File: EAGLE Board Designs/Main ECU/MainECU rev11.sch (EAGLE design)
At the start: 208 parts, among them J1 CONNECTOR-40__, J2 ADIS16460, J3 CONNECTOR-40__, J4 CONNECTOR-40__, J5 CONNECTOR-40__, K1 RELAY_DPDT_RT424024, K10 RELAY_DPDT_RT424024, K11 RELAY_DPDT_RT424024, K12 RELAY_DPDT_RT424024, K9 RELAY_DPDT_RT424024, Q3 TRANSISTOR_P_MOS_SOT-23_DMP30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, Q4 TRANSISTOR_N_MOS__DMG3406L-7, Q5 TRANSISTOR_P_MOS_SOT-23_DMP30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, Q6 TRANSISTOR_N_MOS__DMG3406L-7, U1 VOLTAGE_REGULATOR_SOT-223_3.3V, U2 TCAN1051HQV-Q1, U23 ADC128S022, U3 TCAN1051HQV-Q1, U32 ADC128S022, U33 TCAN1051HQV-Q1, U34 OPAMP_1_CHANNEL_OPA991, U37 OPAMP_1_CHANNEL_OPA991, U38 LOGICGATE_OR, U39 OPAMP_1_CHANNEL_OPA991, U4 TCAN1051HQV-Q1, U41 OPAMP_1_CHANNEL_OPA991, U42 LOGICGATE_OR, U43 OPAMP_1_CHANNEL_OPA991, U44 LOGICGATE_NAND, U45 TCAN1051HQV-Q1, U46 TCAN1051HQV-Q1, U5 ADM8316WBX30, U6 ADC128S022, U7 ADC128S022

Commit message: routing progress
routing progress

routing progress
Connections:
- net +24V: now also J1.15, J1.16; no longer J1.1, J1.2
- net +5V: now also J1.14; no longer J1.3, J1.4
- net CANH_1: now also J1.12, U33.CANH; no longer J3.13
- net CANH_2: now also J1.8; no longer J3.16
- net CANH_3: now also J1.4; no longer J3.19, U33.CANH
- net CANL_1: now also J1.10, U33.CANL; no longer J3.14
- net CANL_2: now also J1.6; no longer J3.17
- net CANL_3: now also J1.2; no longer J3.20, U33.CANL
- net CURRENT: now also U32.IN1
- net CURRENT_EXT: no longer U32.IN1
- net GND: no longer J1.5
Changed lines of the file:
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@@
 <attribute name="DESCRIPTION_2" x="176.53" y="10.16" size="2.54" layer="95"/>
 </instance>
-<instance part="U$8" gate="G$1" x="43.18" y="203.2" smashed="yes">
-<attribute name="VALUE" x="43.18" y="208.28" size="1.778" layer="96" align="bottom-center"/>
+<instance part="U$8" gate="G$1" x="78.74" y="167.64" smashed="yes">
+<attribute name="VALUE" x="78.74" y="172.72" size="1.778" layer="96" align="bottom-center"/>
 </instance>
 <instance part="P46" gate="1" x="160.02" y="203.2" smashed="yes">
@@
 <attribute name="VALUE" x="137.16" y="92.71" size="1.27" layer="96" align="top-center"/>
 </instance>
-<instance part="P70" gate="1" x="50.8" y="203.2" smashed="yes">
-<attribute name="VALUE" x="50.8" y="205.74" size="1.27" layer="96" align="bottom-center"/>
+<instance part="P70" gate="1" x="73.66" y="170.18" smashed="yes">
+<attribute name="VALUE" x="73.66" y="172.72" size="1.27" layer="96" align="bottom-center"/>
 </instance>
 <instance part="J1" gate="G$1" x="30.48" y="200.66" smashed="yes">
@@
 </busses>
 <nets>
-<net name="+24V" class="0">
-<segment>
-<pinref part="U$8" gate="G$1" pin="+24V"/>
-<wire x1="40.64" y1="195.58" x2="43.18" y2="195.58" width="0.1524" layer="91"/>
-<wire x1="43.18" y1="195.58" x2="43.18" y2="198.12" width="0.1524" layer="91"/>
-<wire x1="43.18" y1="198.12" x2="43.18" y2="200.66" width="0.1524" layer="91"/>
-<wire x1="40.64" y1="198.12" x2="43.18" y2="198.12" width="0.1524" layer="91"/>
-<junction x="43.18" y="198.12"/>
-<pinref part="J1" gate="G$1" pin="1"/>
-<pinref part="J1" gate="G$1" pin="2"/>
-</segment>
-</net>
 <net name="LOAD_FR_EXT" class="0">
 <segment>
@@
 <segment>
 <pinref part="P64" gate="1" pin="GND"/>
-<wire x1="40.64" y1="187.96" x2="78.74" y2="187.96" width="0.1524" layer="91"/>
-<pinref part="J1" gate="G$1" pin="5"/>
-<wire x1="78.74" y1="187.96" x2="78.74" y2="157.48" width="0.1524" layer="91"/>
 <pinref part="J1" gate="G$1" pin="22"/>
 <wire x1="78.74" y1="157.48" x2="78.74" y2="154.94" width="0.1524" layer="91"/>
@@
 <pinref part="J1" gate="G$1" pin="17"/>
 <wire x1="40.64" y1="157.48" x2="78.74" y2="157.48" width="0.1524" layer="91"/>
-<junction x="78.74" y="157.48"/>
 </segment>
 <segment>
@@
 <net name="CANH_1" class="0">
 <segment>
-<wire x1="99.06" y1="167.64" x2="106.68" y2="167.64" width="0.1524" layer="91"/>
-<label x="106.68" y="167.64" size="1.27" layer="95" xref="yes"/>
-<pinref part="J3" gate="G$1" pin="13"/>
+<wire x1="40.64" y1="170.18" x2="48.26" y2="170.18" width="0.1524" layer="91"/>
+<label x="48.26" y="170.18" size="1.27" layer="95" xref="yes"/>
+<pinref part="J1" gate="G$1" pin="12"/>
 </segment>
 </net>
 <net name="CANL_1" class="0">
 <segment>
-<wire x1="99.06" y1="165.1" x2="106.68" y2="165.1" width="0.1524" layer="91"/>
-<label x="106.68" y="165.1" size="1.27" layer="95" xref="yes"/>
-<pinref part="J3" gate="G$1" pin="14"/>
+<wire x1="40.64" y1="175.26" x2="48.26" y2="175.26" width="0.1524" layer="91"/>
+<label x="48.26" y="175.26" size="1.27" layer="95" xref="yes"/>
+<pinref part="J1" gate="G$1" pin="10"/>
 </segment>
 </net>
 <net name="CANH_2" class="0">
 <segment>
-<wire x1="99.06" y1="160.02" x2="106.68" y2="160.02" width="0.1524" layer="91"/>
-<label x="106.68" y="160.02" size="1.27" layer="95" xref="yes"/>
-<pinref part="J3" gate="G$1" pin="16"/>
+<wire x1="40.64" y1="180.34" x2="48.26" y2="180.34" width="0.1524" layer="91"/>
+<label x="48.26" y="180.34" size="1.27" layer="95" xref="yes"/>
+<pinref part="J1" gate="G$1" pin="8"/>
 </segment>
 </net>
 <net name="CANL_2" class="0">
 <segment>
-<wire x1="99.06" y1="157.48" x2="106.68" y2="157.48" width="0.1524" layer="91"/>
-<label x="106.68" y="157.48" size="1.27" layer="95" xref="yes"/>
-<pinref part="J3" gate="G$1" pin="17"/>
+<wire x1="40.64" y1="185.42" x2="48.26" y2="185.42" width="0.1524" layer="91"/>
+<label x="48.26" y="185.42" size="1.27" layer="95" xref="yes"/>
+<pinref part="J1" gate="G$1" pin="6"/>
 </segment>
 </net>
 <net name="CANH_3" class="0">
 <segment>
-<wire x1="99.06" y1="152.4" x2="106.68" y2="152.4" width="0.1524" layer="91"/>
-<label x="106.68" y="152.4" size="1.27" layer="95" xref="yes"/>
-<pinref part="J3" gate="G$1" pin="19"/>
+<wire x1="40.64" y1="190.5" x2="48.26" y2="190.5" width="0.1524" layer="91"/>
+<pinref part="J1" gate="G$1" pin="4"/>
+<label x="48.26" y="190.5" size="1.27" layer="95" xref="yes"/>
 </segment>
 </net>
 <net name="CANL_3" class="0">
 <segment>
-<wire x1="99.06" y1="149.86" x2="106.68" y2="149.86" width="0.1524" layer="91"/>
-<label x="106.68" y="149.86" size="1.27" layer="95" xref="yes"/>
-<pinref part="J3" gate="G$1" pin="20"/>
+<wire x1="40.64" y1="195.58" x2="48.26" y2="195.58" width="0.1524" layer="91"/>
+<pinref part="J1" gate="G$1" pin="2"/>
+<label x="48.26" y="195.58" size="1.27" layer="95" xref="yes"/>
 </segment>
 </net>
@@
 <net name="INVERTER_24V_EN" class="0">
 <segment>
-<wire x1="43.18" y1="170.18" x2="50.8" y2="170.18" width="0.1524" layer="91"/>
-<label x="50.8" y="170.18" size="1.27" layer="95" xref="yes"/>
+<wire x1="5.08" y1="236.22" x2="12.7" y2="236.22" width="0.1524" layer="91"/>
+<label x="12.7" y="236.22" size="1.27" layer="95" xref="yes"/>
 </segment>
 </net>
 <net name="INVERTER_TORQUE_EN" class="0">
 <segment>
-<wire x1="43.18" y1="167.64" x2="50.8" y2="167.64" width="0.1524" layer="91"/>
-<label x="50.8" y="167.64" size="1.27" layer="95" xref="yes"/>
+<wire x1="5.08" y1="233.68" x2="12.7" y2="233.68" width="0.1524" layer="91"/>
+<label x="12.7" y="233.68" size="1.27" layer="95" xref="yes"/>
 </segment>
 </net>
 <net name="INVERTER_OUTPUT_EN" class="0">
 <segment>
-<wire x1="43.18" y1="165.1" x2="50.8" y2="165.1" width="0.1524" layer="91"/>
-<label x="50.8" y="165.1" size="1.27" layer="95" xref="yes"/>
+<wire x1="5.08" y1="231.14" x2="12.7" y2="231.14" width="0.1524" layer="91"/>
+<label x="12.7" y="231.14" size="1.27" layer="95" xref="yes"/>
 </segment>
 </net>
 <net name="INVERTER_CTL_EN" class="0">
 <segment>
-<wire x1="43.18" y1="162.56" x2="50.8" y2="162.56" width="0.1524" layer="91"/>
-<label x="50.8" y="162.56" size="1.27" layer="95" xref="yes"/>
+<wire x1="5.08" y1="228.6" x2="12.7" y2="228.6" width="0.1524" layer="91"/>
+<label x="12.7" y="228.6" size="1.27" layer="95" xref="yes"/>
 </segment>
 </net>
 <net name="BRAKE_LIGHT_EN" class="0">
 <segment>
-<wire x1="43.18" y1="160.02" x2="50.8" y2="160.02" width="0.1524" layer="91"/>
-<label x="50.8" y="160.02" size="1.27" layer="95" xref="yes"/>
+<wire x1="5.08" y1="226.06" x2="12.7" y2="226.06" width="0.1524" layer="91"/>
+<label x="12.7" y="226.06" size="1.27" layer="95" xref="yes"/>
 </segment>
 </net>
@@
 </segment>
 <segment>
+<pinref part="J1" gate="G$1" pin="14"/>
 <pinref part="P70" gate="1" pin="+5V"/>
-<wire x1="40.64" y1="193.04" x2="50.8" y2="193.04" width="0.1524" layer="91"/>
-<wire x1="50.8" y1="193.04" x2="50.8" y2="200.66" width="0.1524" layer="91"/>
-<wire x1="40.64" y1="190.5" x2="50.8" y2="190.5" width="0.1524" layer="91"/>
-<wire x1="50.8" y1="190.5" x2="50.8" y2="193.04" width="0.1524" layer="91"/>
-<junction x="50.8" y="193.04"/>
-<pinref part="J1" gate="G$1" pin="3"/>
-<pinref part="J1" gate="G$1" pin="4"/>
+<wire x1="40.64" y1="165.1" x2="73.66" y2="165.1" width="0.1524" layer="91"/>
+<wire x1="73.66" y1="165.1" x2="73.66" y2="167.64" width="0.1524" layer="91"/>
 </segment>
 </net>
@@
 </segment>
 </net>
+<net name="+24V" class="0">
+<segment>
+<pinref part="J1" gate="G$1" pin="16"/>
+<pinref part="U$8" gate="G$1" pin="+24V"/>
+<wire x1="40.64" y1="160.02" x2="78.74" y2="160.02" width="0.1524" layer="91"/>
+<wire x1="78.74" y1="160.02" x2="78.74" y2="162.56" width="0.1524" layer="91"/>
+<pinref part="J1" gate="G$1" pin="15"/>
+<wire x1="78.74" y1="162.56" x2="78.74" y2="165.1" width="0.1524" layer="91"/>
+<wire x1="40.64" y1="162.56" x2="78.74" y2="162.56" width="0.1524" layer="91"/>
+<junction x="78.74" y="162.56"/>
+</segment>
+</net>
 </nets>
 </sheet>
@@
 <net name="CANH_3" class="0">
 <segment>
-<wire x1="60.96" y1="30.48" x2="63.5" y2="30.48" width="0.1524" layer="91"/>
-<label x="63.5" y="30.48" size="1.27" layer="95" xref="yes"/>
-<pinref part="U33" gate="G$1" pin="CANH"/>
-</segment>
-<segment>
 <wire x1="187.96" y1="78.74" x2="190.5" y2="78.74" width="0.1524" layer="91"/>
 <label x="190.5" y="78.74" size="1.27" layer="95" xref="yes"/>
@@
 <net name="CANL_3" class="0">
 <segment>
-<wire x1="60.96" y1="27.94" x2="63.5" y2="27.94" width="0.1524" layer="91"/>
-<label x="63.5" y="27.94" size="1.27" layer="95" xref="yes"/>
-<pinref part="U33" gate="G$1" pin="CANL"/>
-</segment>
-<segment>
 <wire x1="187.96" y1="76.2" x2="190.5" y2="76.2" width="0.1524" layer="91"/>
 <label x="190.5" y="76.2" size="1.27" layer="95" xref="yes"/>
@@
 </segment>
 </net>
-<net name="CURRENT_EXT" class="0">
-<segment>
-<pinref part="U32" gate="G$1" pin="IN1"/>
-<wire x1="251.46" y1="93.98" x2="254" y2="93.98" width="0.1524" layer="91"/>
-<label x="254" y="93.98" size="1.27" layer="95" xref="yes"/>
-</segment>
-</net>
 <net name="TCU_RX4" class="0">
 <segment>
@@
 </segment>
 </net>
+<net name="CANH_1" class="0">
+<segment>
+<wire x1="60.96" y1="30.48" x2="63.5" y2="30.48" width="0.1524" layer="91"/>
+<label x="63.5" y="30.48" size="1.27" layer="95" xref="yes"/>
+<pinref part="U33" gate="G$1" pin="CANH"/>
+</segment>
+</net>
+<net name="CANL_1" class="0">
+<segment>
+<wire x1="60.96" y1="27.94" x2="63.5" y2="27.94" width="0.1524" layer="91"/>
+<label x="63.5" y="27.94" size="1.27" layer="95" xref="yes"/>
+<pinref part="U33" gate="G$1" pin="CANL"/>
+</segment>
+</net>
+<net name="CURRENT" class="0">
+<segment>
+<pinref part="U32" gate="G$1" pin="IN1"/>
+<wire x1="251.46" y1="93.98" x2="254" y2="93.98" width="0.1524" layer="91"/>
+<label x="254" y="93.98" size="1.27" layer="95" xref="yes"/>
+</segment>
+</net>

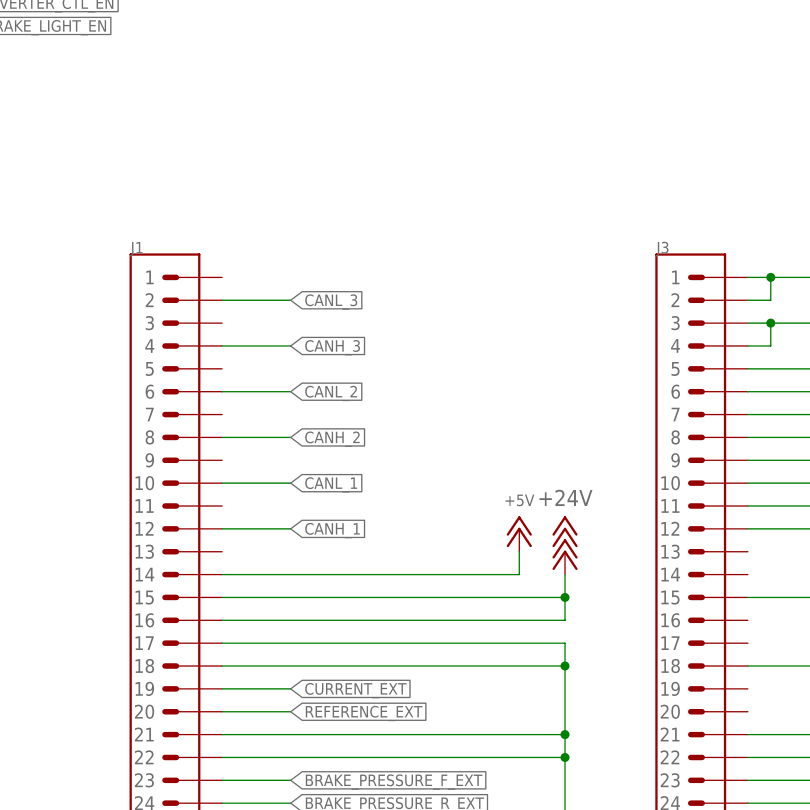
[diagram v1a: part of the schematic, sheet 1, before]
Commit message: changed orientation
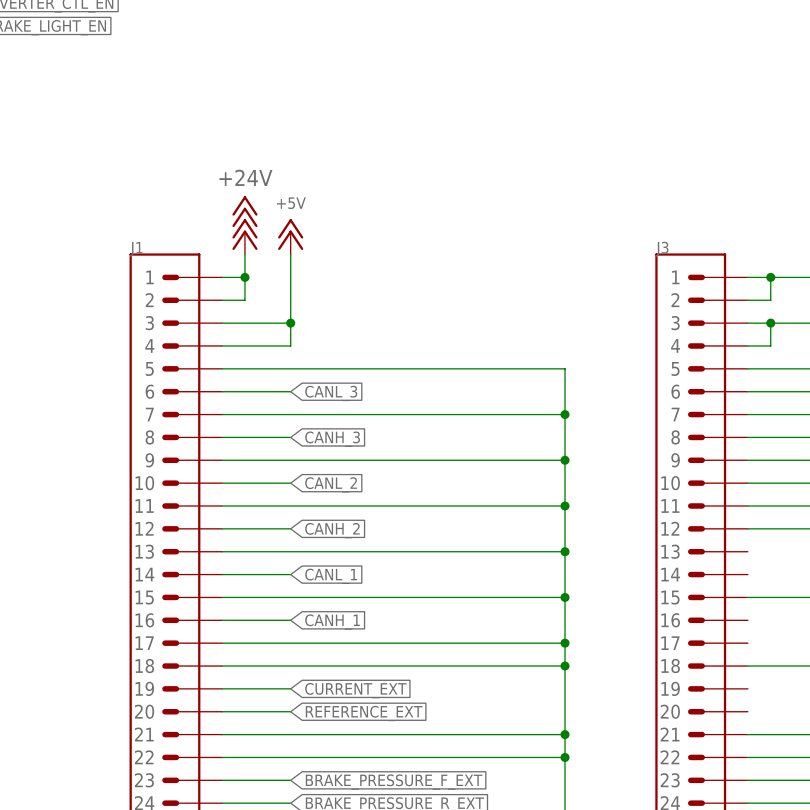
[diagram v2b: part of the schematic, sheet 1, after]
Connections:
- net +24V: now also J1.1, J1.2; no longer J1.15, J1.16
- net +5V: now also J1.3, J1.4; no longer J1.14
- net CANH_1: now also J1.16; no longer J1.12
- net CANH_2: now also J1.12; no longer J1.8
- net CANH_3: now also J1.8; no longer J1.4
- net CANL_1: now also J1.14; no longer J1.10
- net CANL_2: now also J1.10; no longer J1.6
- net CANL_3: now also J1.6; no longer J1.2
- net GND: now also J1.11, J1.13, J1.15, J1.5, J1.7, J1.9
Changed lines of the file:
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@@
 <attribute name="DESCRIPTION_2" x="176.53" y="10.16" size="2.54" layer="95"/>
 </instance>
-<instance part="U$8" gate="G$1" x="78.74" y="167.64" smashed="yes">
-<attribute name="VALUE" x="78.74" y="172.72" size="1.778" layer="96" align="bottom-center"/>
+<instance part="U$8" gate="G$1" x="43.18" y="203.2" smashed="yes">
+<attribute name="VALUE" x="43.18" y="208.28" size="1.778" layer="96" align="bottom-center"/>
 </instance>
 <instance part="P46" gate="1" x="160.02" y="203.2" smashed="yes">
@@
 <attribute name="VALUE" x="137.16" y="92.71" size="1.27" layer="96" align="top-center"/>
 </instance>
-<instance part="P70" gate="1" x="73.66" y="170.18" smashed="yes">
-<attribute name="VALUE" x="73.66" y="172.72" size="1.27" layer="96" align="bottom-center"/>
+<instance part="P70" gate="1" x="48.26" y="203.2" smashed="yes">
+<attribute name="VALUE" x="48.26" y="205.74" size="1.27" layer="96" align="bottom-center"/>
 </instance>
 <instance part="J1" gate="G$1" x="30.48" y="200.66" smashed="yes">
@@
 <pinref part="J1" gate="G$1" pin="17"/>
 <wire x1="40.64" y1="157.48" x2="78.74" y2="157.48" width="0.1524" layer="91"/>
+<pinref part="J1" gate="G$1" pin="5"/>
+<wire x1="40.64" y1="187.96" x2="78.74" y2="187.96" width="0.1524" layer="91"/>
+<wire x1="78.74" y1="187.96" x2="78.74" y2="182.88" width="0.1524" layer="91"/>
+<junction x="78.74" y="157.48"/>
+<pinref part="J1" gate="G$1" pin="7"/>
+<wire x1="78.74" y1="182.88" x2="78.74" y2="177.8" width="0.1524" layer="91"/>
+<wire x1="78.74" y1="177.8" x2="78.74" y2="172.72" width="0.1524" layer="91"/>
+<wire x1="78.74" y1="172.72" x2="78.74" y2="167.64" width="0.1524" layer="91"/>
+<wire x1="78.74" y1="167.64" x2="78.74" y2="162.56" width="0.1524" layer="91"/>
+<wire x1="78.74" y1="162.56" x2="78.74" y2="157.48" width="0.1524" layer="91"/>
+<wire x1="40.64" y1="182.88" x2="78.74" y2="182.88" width="0.1524" layer="91"/>
+<junction x="78.74" y="182.88"/>
+<pinref part="J1" gate="G$1" pin="9"/>
+<wire x1="40.64" y1="177.8" x2="78.74" y2="177.8" width="0.1524" layer="91"/>
+<junction x="78.74" y="177.8"/>
+<pinref part="J1" gate="G$1" pin="11"/>
+<wire x1="40.64" y1="172.72" x2="78.74" y2="172.72" width="0.1524" layer="91"/>
+<junction x="78.74" y="172.72"/>
+<pinref part="J1" gate="G$1" pin="13"/>
+<wire x1="40.64" y1="167.64" x2="78.74" y2="167.64" width="0.1524" layer="91"/>
+<junction x="78.74" y="167.64"/>
+<pinref part="J1" gate="G$1" pin="15"/>
+<wire x1="40.64" y1="162.56" x2="78.74" y2="162.56" width="0.1524" layer="91"/>
+<junction x="78.74" y="162.56"/>
 </segment>
 <segment>
@@
 <net name="CANH_1" class="0">
 <segment>
+<wire x1="40.64" y1="160.02" x2="48.26" y2="160.02" width="0.1524" layer="91"/>
+<label x="48.26" y="160.02" size="1.27" layer="95" xref="yes"/>
+<pinref part="J1" gate="G$1" pin="16"/>
+</segment>
+</net>
+<net name="CANL_1" class="0">
+<segment>
+<wire x1="40.64" y1="165.1" x2="48.26" y2="165.1" width="0.1524" layer="91"/>
+<label x="48.26" y="165.1" size="1.27" layer="95" xref="yes"/>
+<pinref part="J1" gate="G$1" pin="14"/>
+</segment>
+</net>
+<net name="CANH_2" class="0">
+<segment>
 <wire x1="40.64" y1="170.18" x2="48.26" y2="170.18" width="0.1524" layer="91"/>
 <label x="48.26" y="170.18" size="1.27" layer="95" xref="yes"/>
@@
 </segment>
 </net>
-<net name="CANL_1" class="0">
+<net name="CANL_2" class="0">
 <segment>
 <wire x1="40.64" y1="175.26" x2="48.26" y2="175.26" width="0.1524" layer="91"/>
@@
 </segment>
 </net>
-<net name="CANH_2" class="0">
+<net name="CANH_3" class="0">
 <segment>
 <wire x1="40.64" y1="180.34" x2="48.26" y2="180.34" width="0.1524" layer="91"/>
@@
 </segment>
 </net>
-<net name="CANL_2" class="0">
+<net name="CANL_3" class="0">
 <segment>
 <wire x1="40.64" y1="185.42" x2="48.26" y2="185.42" width="0.1524" layer="91"/>
 <label x="48.26" y="185.42" size="1.27" layer="95" xref="yes"/>
 <pinref part="J1" gate="G$1" pin="6"/>
-</segment>
-</net>
-<net name="CANH_3" class="0">
-<segment>
-<wire x1="40.64" y1="190.5" x2="48.26" y2="190.5" width="0.1524" layer="91"/>
-<pinref part="J1" gate="G$1" pin="4"/>
-<label x="48.26" y="190.5" size="1.27" layer="95" xref="yes"/>
-</segment>
-</net>
-<net name="CANL_3" class="0">
-<segment>
-<wire x1="40.64" y1="195.58" x2="48.26" y2="195.58" width="0.1524" layer="91"/>
-<pinref part="J1" gate="G$1" pin="2"/>
-<label x="48.26" y="195.58" size="1.27" layer="95" xref="yes"/>
 </segment>
 </net>
@@
 </segment>
 <segment>
-<pinref part="J1" gate="G$1" pin="14"/>
+<pinref part="J1" gate="G$1" pin="3"/>
 <pinref part="P70" gate="1" pin="+5V"/>
-<wire x1="40.64" y1="165.1" x2="73.66" y2="165.1" width="0.1524" layer="91"/>
-<wire x1="73.66" y1="165.1" x2="73.66" y2="167.64" width="0.1524" layer="91"/>
+<wire x1="40.64" y1="193.04" x2="48.26" y2="193.04" width="0.1524" layer="91"/>
+<wire x1="48.26" y1="193.04" x2="48.26" y2="200.66" width="0.1524" layer="91"/>
+<pinref part="J1" gate="G$1" pin="4"/>
+<wire x1="40.64" y1="190.5" x2="48.26" y2="190.5" width="0.1524" layer="91"/>
+<wire x1="48.26" y1="190.5" x2="48.26" y2="193.04" width="0.1524" layer="91"/>
+<junction x="48.26" y="193.04"/>
 </segment>
 </net>
@@
 <net name="+24V" class="0">
 <segment>
-<pinref part="J1" gate="G$1" pin="16"/>
+<pinref part="J1" gate="G$1" pin="2"/>
 <pinref part="U$8" gate="G$1" pin="+24V"/>
-<wire x1="40.64" y1="160.02" x2="78.74" y2="160.02" width="0.1524" layer="91"/>
-<wire x1="78.74" y1="160.02" x2="78.74" y2="162.56" width="0.1524" layer="91"/>
-<pinref part="J1" gate="G$1" pin="15"/>
-<wire x1="78.74" y1="162.56" x2="78.74" y2="165.1" width="0.1524" layer="91"/>
-<wire x1="40.64" y1="162.56" x2="78.74" y2="162.56" width="0.1524" layer="91"/>
-<junction x="78.74" y="162.56"/>
-</segment>
-</net>
+<wire x1="40.64" y1="195.58" x2="43.18" y2="195.58" width="0.1524" layer="91"/>
+<wire x1="43.18" y1="195.58" x2="43.18" y2="198.12" width="0.1524" layer="91"/>
+<pinref part="J1" gate="G$1" pin="1"/>
+<wire x1="43.18" y1="198.12" x2="43.18" y2="200.66" width="0.1524" layer="91"/>
+<wire x1="40.64" y1="198.12" x2="43.18" y2="198.12" width="0.1524" layer="91"/>
+<junction x="43.18" y="198.12"/>
+</segment>
+</net>

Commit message: routing progress
routing progress
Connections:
- removed net BRAKELIGHT_CONTROL: A2.D2
- removed net INVERTER_CONTROLLER_EN: A2.A14
- removed net INVERTER_CTL: A2.A17
- new net BRAKELIGHT_EN: A2.D6, J3.9
- new net INVERTER_24V_EN: A2.D7, J3.12
- new net INVERTER_CTL_EN: A2.(CS)D10, J3.13
- net !AD1_CS: now also A2.A17; no longer A2.(CS)D10
- net !AD2_CS: now also A2.A16; no longer A2.D9
- net !AD3_CS: now also A2.A15; no longer A2.D8
- net !IMU_CS: now also A2.D3; no longer A2.A1
- net !IMU_RESET: now also A2.D2; no longer A2.A4
- net BMS_OK: now also J3.24; no longer J3.3, J3.4
- net BOTS_SENSE: now also A2.D29; no longer A2.D37
- net BOTS_SENSE_EXT: now also J3.21; no longer J3.10
- net FL_INTERLOCK_SENSE: now also A2.A11; no longer A2.D33
- net FL_INTERLOCK_SENSE_EXT: now also J3.17; no longer J3.6
- net FR_INTERLOCK_SENSE: now also A2.A10; no longer A2.D34
- net FR_INTERLOCK_SENSE_EXT: now also J3.18; no longer J3.7
- net GND: now also J3.25, J3.26, J3.35, J3.36; no longer J3.12, J3.15, J3.18, J3.21, J3.30, J3.5
- net IMU_DATAREADY: now also A2.D5; no longer A2.A3
- net IMU_SYNC: now also A2.D4; no longer A2.A2
- net INERTIA_SENSE: now also A2.D28; no longer A2.D32
- net INERTIA_SENSE_EXT: now also J3.22; no longer J3.11
- net INVERTER_OUTPUT_STAGE_EN: now also A2.D9, J3.14; no longer A2.A16
- net INVERTER_TORQUE_LIMIT_EN: now also A2.D8, J3.11; no longer A2.A15
- net OKHS_IN: now also J3.23; no longer J3.1, J3.2
- net RL_INTERLOCK_SENSE: now also A2.A13; no longer A2.D35
- net RL_INTERLOCK_SENSE_EXT: now also J3.19; no longer J3.8
- net RR_INTERLOCK_SENSE: now also A2.A12; no longer A2.D36
- net RR_INTERLOCK_SENSE_EXT: now also J3.20; no longer J3.9
- net SHDN_B_READ: now also A2.D33; no longer A2.D3
- net SHDN_C_READ: now also A2.D34; no longer A2.D4
- net SHDN_D_READ: now also A2.D35; no longer A2.D5
- net SHDN_E_READ: now also A2.D36; no longer A2.D6
- net SOFTWARE_OK: now also A2.A6; no longer A2.A0
- net TCU_RX4: now also J3.29; no longer J3.22
- net TCU_RX5: now also J3.28; no longer J3.24
- net TCU_RX6: now also J3.31; no longer J3.26
- net TCU_RX7: now also J3.34; no longer J3.28
- net TCU_TX4: now also J3.30; no longer J3.23
- net TCU_TX5: now also J3.27; no longer J3.25
- net TCU_TX6: now also J3.32; no longer J3.27
- net TCU_TX7: now also J3.33; no longer J3.29
- net WATCHDOG: now also A2.A7; no longer A2.D7
